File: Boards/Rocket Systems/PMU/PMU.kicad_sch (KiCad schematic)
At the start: 134 parts, among them IC1 LM4040DIZ-4.1_NOPB, IC2 LM4040DIZ-4.1_NOPB, IC3 LM4040DIZ-4.1_NOPB, IC4 LS1205EFD33, J1 2200981271, J2 XT30UPB-F, J3 XT30UPB-F, J4 XT30UPB-F, J5 XT30UPB-F, J7 Conn_01x04_Pin, J8 Conn_01x02_Pin, K3 G3VM-31DR_TR05_, K4 G3VM-31DR_TR05_, K5 G3VM-31DR_TR05_, Q1 NPN, Q2 PMOS, Q3 NPN, Q4 NPN, Q5 NPN, Q6 NPN, Q7 NPN, Q8 NPN, U10 ST1L05APU33R, U29 NCV8114ASN165T1G, U3 STPS15L45CB, U30 MCP6002-E/MS, U4 STPS15L45CB, U7 NJD35N04T4G, U8 NJD35N04T4G, U9 NJD35N04T4G

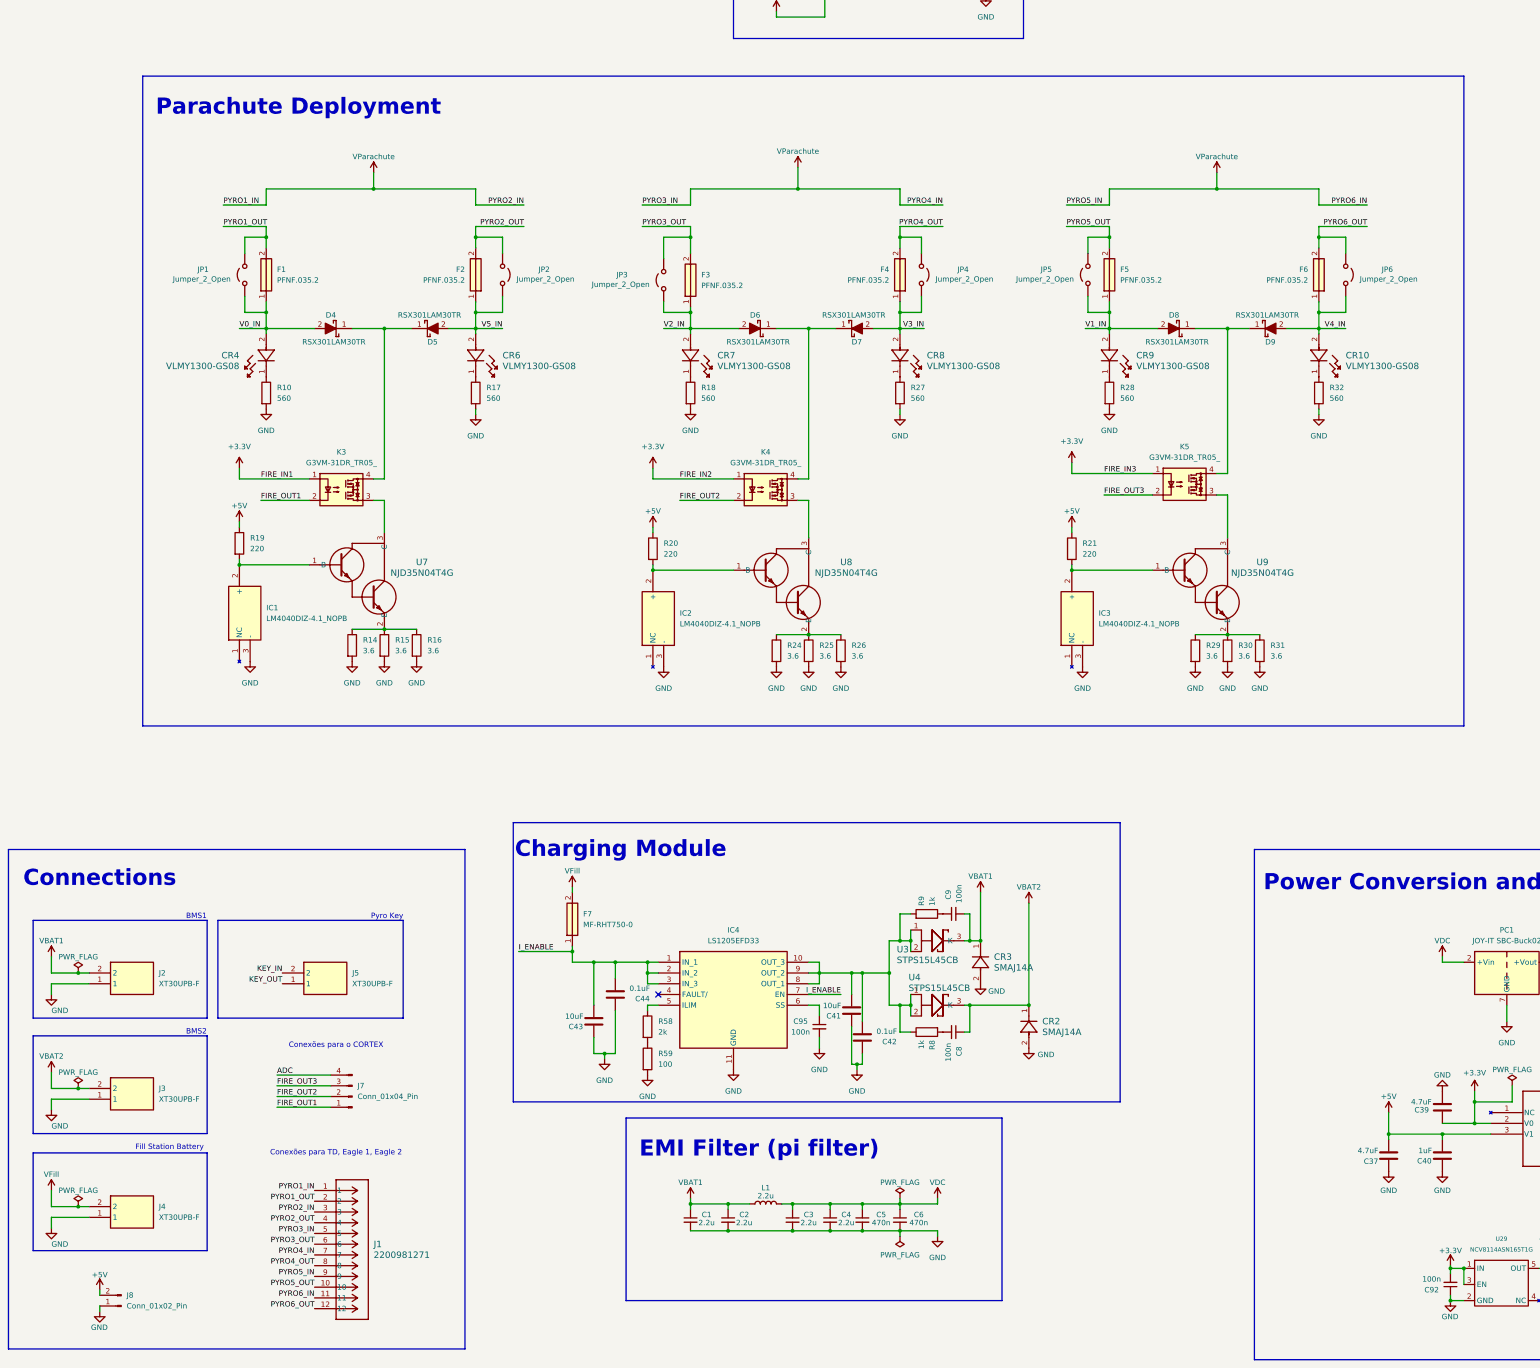
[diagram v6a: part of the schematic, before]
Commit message: PMU layout
Full layout
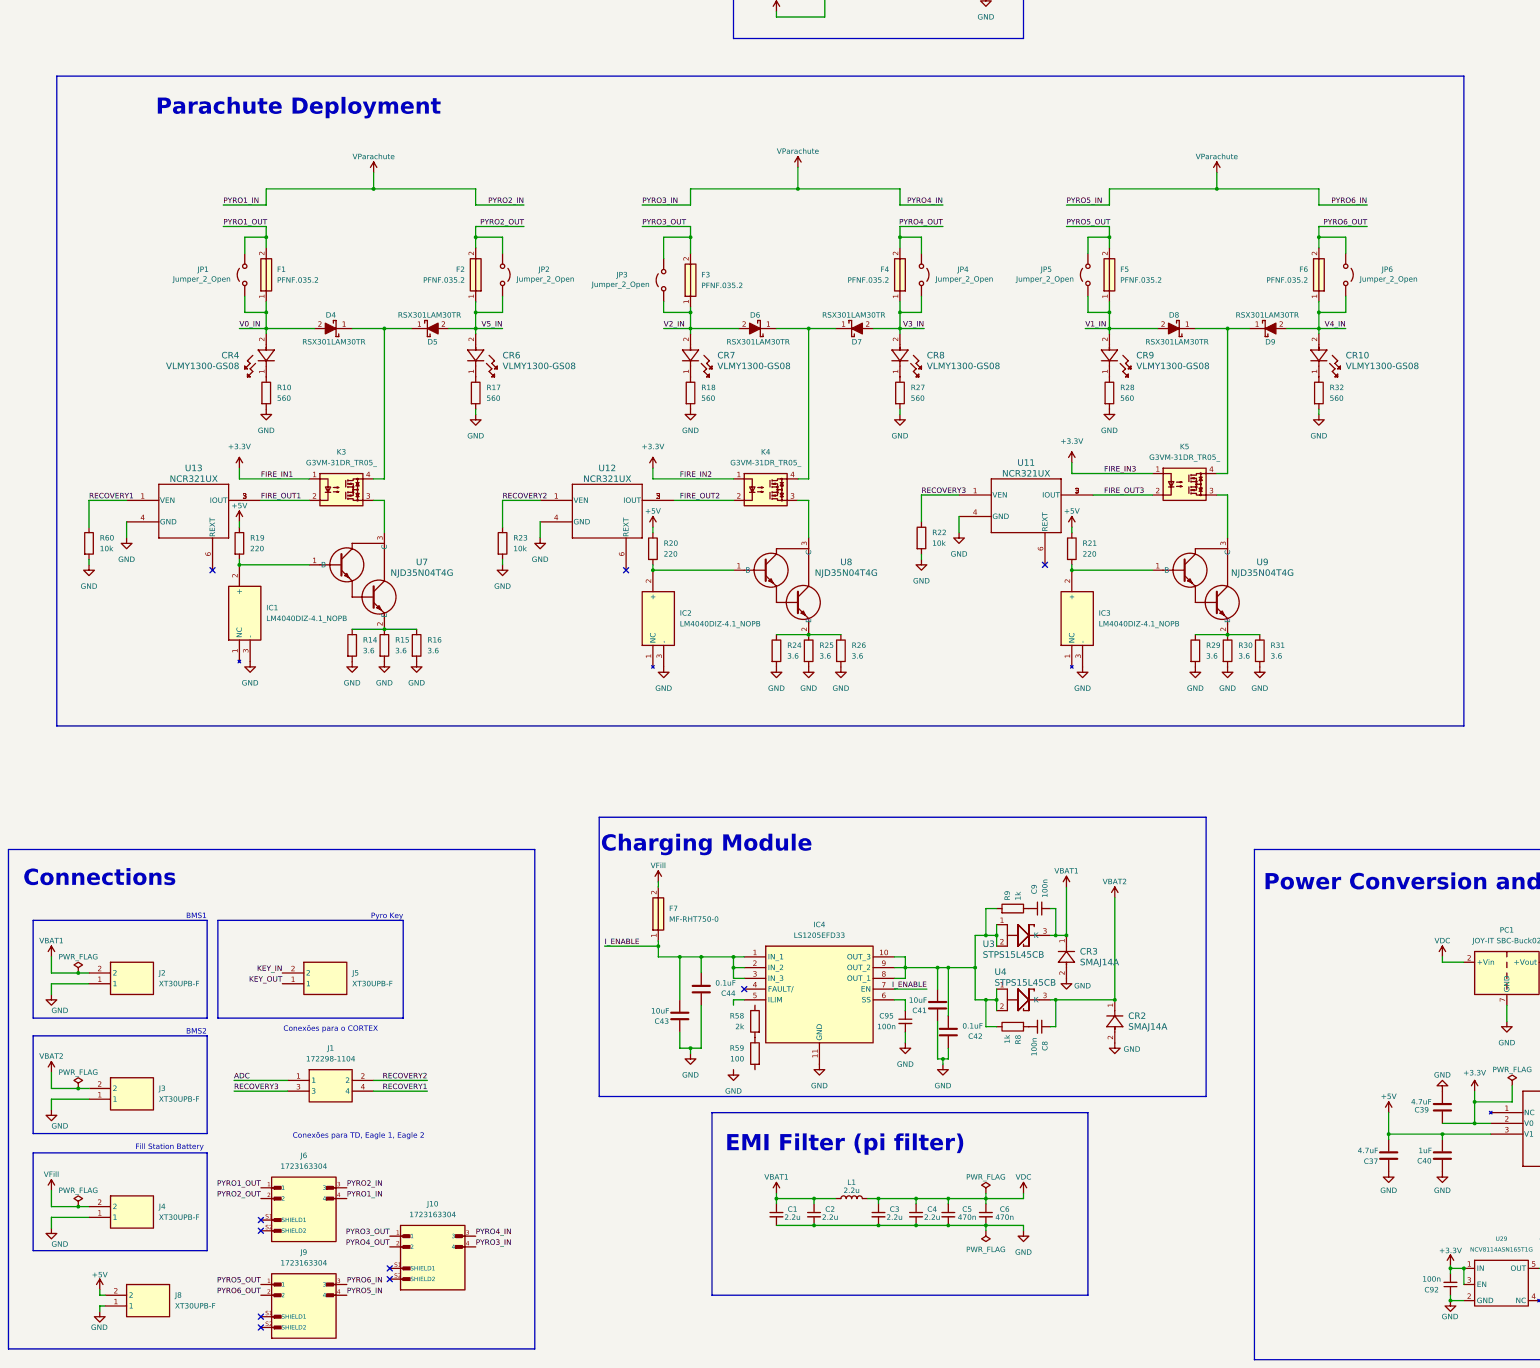
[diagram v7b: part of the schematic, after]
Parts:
- removed J1: 2200981271, 2200981271:CONN_2200980000-SD_12_MOL, symbol 2200981271:2200981271
- removed J7: Conn_01x04_Pin, symbol Connector:Conn_01x04_Pin
- removed J8: Conn_01x02_Pin, symbol Connector:Conn_01x02_Pin
- added J1: 172298-1104, 172298-YY04, symbol 172298-1104:172298-1104
- added J10, J6, J9: 1723163304, 1723163304:MOLEX_1723163304, symbol 1723163304:1723163304
- added J8: XT30UPB-F, XT30UPB-F:XT30UPBF, symbol XT30UPB-F:XT30UPB-F
- added R22, R23, R60: 10k, Resistor-0402:RES_0402, symbol Device:R
- added U11, U12, U13: NCR321UX, LED Driver_NCR321UX:TSOP6_SOT457_NEX, symbol NCR321UX:NCR321UX
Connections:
- net +5V: now also J8.2
- net ADC: now also J1.1
- net FIRE_OUT1: now also U13.2 (IOUT), U13.3 (IOUT), U13.5 (IOUT)
- net FIRE_OUT2: now also U12.2 (IOUT), U12.3 (IOUT), U12.5 (IOUT)
- net FIRE_OUT3: now also U11.2 (IOUT), U11.3 (IOUT), U11.5 (IOUT)
- net GND: now also J8.1, R22.2, R23.2, R60.2, U11.4 (GND), U12.4 (GND), U13.4 (GND); no longer R59.2
- net PYRO1_OUT: now also J6.1
- net PYRO2_OUT: now also J6.2
- net PYRO3_OUT: now also J10.1
- net PYRO4_OUT: now also J10.2
- net PYRO5_OUT: now also J9.1
- net PYRO6_OUT: now also J9.2
- net VParachute: now also J10.3, J10.4, J6.3, J6.4, J9.3, J9.4
- net at R58.1: no longer IC4.5 (ILIM)
- new net RECOVERY1: J1.4, R60.1, U13.1 (VEN)
- new net RECOVERY2: J1.2, R23.1, U12.1 (VEN)
- new net RECOVERY3: J1.3, R22.1, U11.1 (VEN)
- no-connect marks 1 -> 10
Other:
- moved on the sheet: C1, C2, C3, C4, C41, C42, C43, C44, C5, C6, C8, C9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

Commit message: PMU
basicamente feito
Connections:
- net GND: now also R59.2
- net RECOVERY2: now also J1.3; no longer J1.2
- net RECOVERY3: now also J1.2; no longer J1.3
- net at R58.1: now also IC4.5 (ILIM)
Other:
- moved on the sheet: R58, R59
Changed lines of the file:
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@@
 	)
 	(label "RECOVERY3"
-		(at 85.09 331.47 0)
+		(at 130.81 328.93 180)
 		(effects
 			(font
 				(size 1.27 1.27)
 			)
-			(justify left bottom)
+			(justify right bottom)
 		)
 	)
@@
 	)
 	(label "RECOVERY2"
-		(at 130.81 328.93 180)
+		(at 85.09 331.47 0)
 		(effects
 			(font
 				(size 1.27 1.27)
 			)
-			(justify right bottom)
+			(justify left bottom)
 		)
 	)
@@
 	(symbol
 		(lib_id "Device:R")
-		(at 208.28 322.58 0)
+		(at 203.2 322.58 0)
 		(mirror y)
 		(unit 1)
@@
 		(fields_autoplaced yes)
 		(property "Reference" "R59"
-			(at 205.74 321.3099 0)
+			(at 200.66 321.3099 0)
 			(effects
 				(font
@@
 		)
 		(property "Value" "100"
-			(at 205.74 323.8499 0)
+			(at 200.66 323.8499 0)
 			(effects
 				(font
@@
 		)
 		(property "Footprint" "Resistor-0603:RES_0603"
-			(at 210.058 322.58 90)
+			(at 204.978 322.58 90)
 			(effects
 				(font
@@
 		)
 		(property "Datasheet" "~"
-			(at 208.28 322.58 0)
+			(at 203.2 322.58 0)
 			(effects
 				(font
@@
 		)
 		(property "Description" "Resistor"
-			(at 208.28 322.58 0)
+			(at 203.2 322.58 0)
 			(effects
 				(font
@@
 	(symbol
 		(lib_id "Device:R")
-		(at 208.28 314.96 0)
+		(at 203.2 314.96 0)
 		(mirror y)
 		(unit 1)
@@
 		(fields_autoplaced yes)
 		(property "Reference" "R58"
-			(at 205.74 313.6899 0)
+			(at 200.66 313.6899 0)
 			(effects
 				(font
@@
 		)
 		(property "Value" "2k"
-			(at 205.74 316.2299 0)
+			(at 200.66 316.2299 0)
 			(effects
 				(font
@@
 		)
 		(property "Footprint" "Resistor-0603:RES_0603"
-			(at 210.058 314.96 90)
+			(at 204.978 314.96 90)
 			(effects
 				(font
@@
 		)
 		(property "Datasheet" "~"
-			(at 208.28 314.96 0)
+			(at 203.2 314.96 0)
 			(effects
 				(font
@@
 		)
 		(property "Description" "Resistor"
-			(at 208.28 314.96 0)
+			(at 203.2 314.96 0)
 			(effects
 				(font
